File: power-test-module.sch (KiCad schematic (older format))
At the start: 2 parts, among them J3 Conn_01x06, J4 Conn_01x06

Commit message: fixed design-rule issues
 - removed stray via
 - replaced 2 single-row headers by a 2x6 (vertical) header to
   avoid court-yard overlaps.
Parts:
- removed J3, J4: Conn_01x06, Connector_PinHeader_2.54mm:PinHeader_1x06_P2.54mm_Horizontal, symbol Connector_Generic:Conn_01x06
- added J3: Conn_02x06_Odd_Even, Connector_PinHeader_2.54mm:PinHeader_2x06_P2.54mm_Vertical, symbol Connector_Generic:Conn_02x06_Odd_Even
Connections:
- wire segments 17 -> 24
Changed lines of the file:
@@
 $EndSheet
 Wire Wire Line
-	3750 4600 3400 4600
-Wire Wire Line
-	3400 4700 3750 4700
-$Comp
-L power:+3V3 #PWR?
-U 1 1 5C4DEBEA
-P 3750 4300
-AR Path="/5BE73D36/5C4DEBEA" Ref="#PWR?"  Part="1"
-AR Path="/5C1147CA/5C4DEBEA" Ref="#PWR?"  Part="1"
-AR Path="/5C4DEBEA" Ref="#PWR?"  Part="1"
-AR Path="/5C4CE703/5C4DEBEA" Ref="#PWR?"  Part="1"
-F 0 "#PWR?" H 3750 4150 50  0001 C CNN
-F 1 "+3V3" H 3765 4473 50  0000 C CNN
-F 2 "" H 3750 4300 50  0001 C CNN
-F 3 "" H 3750 4300 50  0001 C CNN
-	1    3750 4300
-	1    0    0    -1
-$EndComp
+	2150 3600 1800 3600
+Wire Wire Line
+	1800 3700 2150 3700
 $Comp
 L power:+5V #PWR?
@@
 $EndComp
 $Comp
-L power:+5V #PWR?
-U 1 1 5C4DEC0E
-P 4300 5050
-AR Path="/5C1147CA/5C4DEC0E" Ref="#PWR?"  Part="1"
-AR Path="/5CEAC2F1/5C4DEC0E" Ref="#PWR?"  Part="1"
-AR Path="/5C3C60AE/5C4DEC0E" Ref="#PWR?"  Part="1"
-AR Path="/5C4DEC0E" Ref="#PWR?"  Part="1"
-AR Path="/5C4CE703/5C4DEC0E" Ref="#PWR?"  Part="1"
-F 0 "#PWR?" H 4300 4900 50  0001 C CNN
-F 1 "+5V" H 4315 5223 50  0000 C CNN
-F 2 "" H 4300 5050 50  0001 C CNN
-F 3 "" H 4300 5050 50  0001 C CNN
-	1    4300 5050
-	1    0    0    -1
-$EndComp
-$Comp
 L power:+3V3 #PWR?
 U 1 1 5C4DEC14
@@
 Wire Wire Line
 	5350 4750 4950 4750
-Text Notes 3400 4600 0    25   ~ 0
+Text Notes 1800 3600 0    25   ~ 0
 TXD -> Output
-Text Notes 3400 4700 0    25   ~ 0
+Text Notes 1800 3700 0    25   ~ 0
 RXD <- Input
-Wire Wire Line
-	3750 4400 3750 4300
-Wire Wire Line
-	3750 4500 3750 4400
-Connection ~ 3750 4400
-$Comp
-L Connector_Generic:Conn_01x06 J?
-U 1 1 5C4DEC22
-P 3950 4600
-AR Path="/5C4CE703/5C4DEC22" Ref="J?"  Part="1"
-AR Path="/5C4DEC22" Ref="J3"  Part="1"
-F 0 "J3" H 4030 4592 50  0000 L CNN
-F 1 "Conn_01x06" H 4030 4501 50  0000 L CNN
-F 2 "Connector_PinHeader_2.54mm:PinHeader_1x06_P2.54mm_Horizontal" H 3950 4600 50  0001 C CNN
-F 3 "~" H 3950 4600 50  0001 C CNN
-F 4 "Sullins" H 3950 4600 50  0001 C CNN "Manufacturer"
-F 5 "S5481-ND" H 3950 4600 50  0001 C CNN "Part"
-	1    3950 4600
-	1    0    0    -1
-$EndComp
-Wire Wire Line
-	3750 4800 3650 4800
-Wire Wire Line
-	3650 4800 3650 5000
-Wire Wire Line
-	3750 4900 3750 5000
-Wire Wire Line
-	3750 5050 4300 5050
-$Comp
-L Connector_Generic:Conn_01x06 J?
-U 1 1 5C4DEC2F
-P 4800 3650
-AR Path="/5C4CE703/5C4DEC2F" Ref="J?"  Part="1"
-AR Path="/5C4DEC2F" Ref="J4"  Part="1"
-F 0 "J4" H 4880 3642 50  0000 L CNN
-F 1 "Conn_01x06" H 4880 3551 50  0000 L CNN
-F 2 "Connector_PinHeader_2.54mm:PinHeader_1x06_P2.54mm_Horizontal" H 4800 3650 50  0001 C CNN
-F 3 "~" H 4800 3650 50  0001 C CNN
-F 4 "Sullins" H 4800 3650 50  0001 C CNN "Manufacturer"
-F 5 "S5481-ND" H 4800 3650 50  0001 C CNN "Part"
-	1    4800 3650
-	1    0    0    -1
-$EndComp
-Wire Wire Line
-	3650 5000 3750 5000
-Connection ~ 3750 5000
-Wire Wire Line
-	3750 5000 3750 5050
-$Comp
-L power:GND #PWR?
-U 1 1 5C4DEC39
-P 4600 4100
-AR Path="/5C3C60AE/5C4DEC39" Ref="#PWR?"  Part="1"
-AR Path="/5C4DEC39" Ref="#PWR?"  Part="1"
-AR Path="/5C4CE703/5C4DEC39" Ref="#PWR?"  Part="1"
-F 0 "#PWR?" H 4600 3850 50  0001 C CNN
-F 1 "GND" H 4605 3927 50  0000 C CNN
-F 2 "" H 4600 4100 50  0001 C CNN
-F 3 "" H 4600 4100 50  0001 C CNN
-	1    4600 4100
-	1    0    0    -1
-$EndComp
-Wire Wire Line
-	4600 3450 4600 3550
-Connection ~ 4600 3550
-Wire Wire Line
-	4600 3550 4600 3650
-Connection ~ 4600 3650
-Wire Wire Line
-	4600 3650 4600 3750
-Connection ~ 4600 3750
-Wire Wire Line
-	4600 3750 4600 3850
-Connection ~ 4600 3850
-Wire Wire Line
-	4600 3850 4600 3950
-Connection ~ 4600 3950
-Wire Wire Line
-	4600 3950 4600 4100
-Text GLabel 3400 4600 0    50   Input ~ 0
+Text GLabel 1800 3600 0    50   Input ~ 0
 UART_RX_MIO14
-Text GLabel 3400 4700 0    50   Output ~ 0
+Text GLabel 1800 3700 0    50   Output ~ 0
 UART_TX_MIO15
 $Comp
@@
 	1    0    0    -1
 $EndComp
+$Comp
+L Connector_Generic:Conn_02x06_Odd_Even J3
+U 1 1 60D32371
+P 2350 3600
+F 0 "J3" H 2400 4017 50  0000 C CNN
+F 1 "Conn_02x06_Odd_Even" H 3150 3600 50  0000 C CNN
+F 2 "Connector_PinHeader_2.54mm:PinHeader_2x06_P2.54mm_Vertical" H 2350 3600 50  0001 C CNN
+F 3 "~" H 2350 3600 50  0001 C CNN
+	1    2350 3600
+	1    0    0    -1
+$EndComp
+$Comp
+L power:+3V3 #PWR?
+U 1 1 60D34AD1
+P 2100 3250
+AR Path="/5BE73D36/60D34AD1" Ref="#PWR?"  Part="1"
+AR Path="/5C1147CA/60D34AD1" Ref="#PWR?"  Part="1"
+AR Path="/60D34AD1" Ref="#PWR?"  Part="1"
+AR Path="/5C4CE703/60D34AD1" Ref="#PWR?"  Part="1"
+F 0 "#PWR?" H 2100 3100 50  0001 C CNN
+F 1 "+3V3" H 2115 3423 50  0000 C CNN
+F 2 "" H 2100 3250 50  0001 C CNN
+F 3 "" H 2100 3250 50  0001 C CNN
+	1    2100 3250
+	1    0    0    -1
+$EndComp
+Wire Wire Line
+	2100 3250 2100 3400
+Wire Wire Line
+	2100 3500 2150 3500
+Wire Wire Line
+	2150 3400 2100 3400
+Connection ~ 2100 3400
+Wire Wire Line
+	2100 3400 2100 3500
+$Comp
+L power:GND #PWR?
+U 1 1 60D37922
+P 2700 4000
+AR Path="/5C3C60AE/60D37922" Ref="#PWR?"  Part="1"
+AR Path="/60D37922" Ref="#PWR?"  Part="1"
+AR Path="/5C4CE703/60D37922" Ref="#PWR?"  Part="1"
+F 0 "#PWR?" H 2700 3750 50  0001 C CNN
+F 1 "GND" H 2705 3827 50  0000 C CNN
+F 2 "" H 2700 4000 50  0001 C CNN
+F 3 "" H 2700 4000 50  0001 C CNN
+	1    2700 4000
+	1    0    0    -1
+$EndComp
+Wire Wire Line
+	2650 3400 2700 3400
+Wire Wire Line
+	2700 3400 2700 3500
+Wire Wire Line
+	2650 3900 2700 3900
+Connection ~ 2700 3900
+Wire Wire Line
+	2700 3900 2700 4000
+Wire Wire Line
+	2650 3800 2700 3800
+Connection ~ 2700 3800
+Wire Wire Line
+	2700 3800 2700 3900
+Wire Wire Line
+	2650 3700 2700 3700
+Connection ~ 2700 3700
+Wire Wire Line
+	2700 3700 2700 3800
+Wire Wire Line
+	2650 3600 2700 3600
+Connection ~ 2700 3600
+Wire Wire Line
+	2700 3600 2700 3700
+Wire Wire Line
+	2650 3500 2700 3500
+Connection ~ 2700 3500
+Wire Wire Line
+	2700 3500 2700 3600
+$Comp
+L power:+5V #PWR?
+U 1 1 60D397E5
+P 1650 4150
+AR Path="/5C1147CA/60D397E5" Ref="#PWR?"  Part="1"
+AR Path="/5CEAC2F1/60D397E5" Ref="#PWR?"  Part="1"
+AR Path="/5C3C60AE/60D397E5" Ref="#PWR?"  Part="1"
+AR Path="/60D397E5" Ref="#PWR?"  Part="1"
+AR Path="/5C4CE703/60D397E5" Ref="#PWR?"  Part="1"
+F 0 "#PWR?" H 1650 4000 50  0001 C CNN
+F 1 "+5V" H 1665 4323 50  0000 C CNN
+F 2 "" H 1650 4150 50  0001 C CNN
+F 3 "" H 1650 4150 50  0001 C CNN
+	1    1650 4150
+	1    0    0    -1
+$EndComp
+Wire Wire Line
+	2150 3800 2100 3800
+Wire Wire Line
+	2100 3800 2100 3900
+Wire Wire Line
+	2100 4150 1650 4150
+Wire Wire Line
+	2100 3900 2150 3900
+Connection ~ 2100 3900
+Wire Wire Line
+	2100 3900 2100 4150
 $EndSCHEMATC

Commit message: re-annotated with base number 1000
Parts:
- renumbered J3 to J1001
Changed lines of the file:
@@
 $EndComp
 $Comp
-L Connector_Generic:Conn_02x06_Odd_Even J3
+L Connector_Generic:Conn_02x06_Odd_Even J1001
 U 1 1 60D32371
 P 2350 3600
-F 0 "J3" H 2400 4017 50  0000 C CNN
+F 0 "J1001" H 2400 4017 50  0000 C CNN
 F 1 "Conn_02x06_Odd_Even" H 3150 3600 50  0000 C CNN
 F 2 "Connector_PinHeader_2.54mm:PinHeader_2x06_P2.54mm_Vertical" H 2350 3600 50  0001 C CNN

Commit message: use hierarchical labels from power-and-uart sheet
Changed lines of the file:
@@
 F0 "Sheet5C4CE702" 50
 F1 "power-and-uart.sch" 50
+F2 "UART_TX_OUT" O R 5450 1900 50
+F3 "UART_RX_IN" I L 4100 1900 50
 $EndSheet
 Wire Wire Line
@@
 Wire Wire Line
 	2100 3900 2100 4150
+Text GLabel 5750 1900 2    50   Output ~ 0
+UART_RX_MIO14
+Text GLabel 3700 1900 0    50   Input ~ 0
+UART_TX_MIO15
+Wire Wire Line
+	3700 1900 4100 1900
+Wire Wire Line
+	5450 1900 5750 1900
 $EndSCHEMATC

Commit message: use special +5/+3V3 labels with more specific net names
This allows easier integration since these are global labels
and using more specific names helps avoiding clashes.

The labels are stored in the 'rescue' library.

Strangely: the same trick did not work for GND. Kicad always
insists the net name remains 'GND' (it does work, however if
a new schematic is created - then the different net name for
GND 'sticks').
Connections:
- net +3V3 renamed +3V3_PWR_OUT
- net +5V renamed +5V_PWR_OUT
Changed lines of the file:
@@
 	1800 3700 2150 3700
 $Comp
-L power:+5V #PWR?
+L power-test-module-rescue:+5V #PWR?
 U 1 1 5C4DEBF0
 P 7050 4350
@@
 	1    0    0    -1
 $EndComp
-$Comp
-L power:+3V3 #PWR?
-U 1 1 5C4DEC14
-P 5350 4750
-AR Path="/5BE73D36/5C4DEC14" Ref="#PWR?"  Part="1"
-AR Path="/5C1147CA/5C4DEC14" Ref="#PWR?"  Part="1"
-AR Path="/5C4DEC14" Ref="#PWR?"  Part="1"
-AR Path="/5C4CE703/5C4DEC14" Ref="#PWR?"  Part="1"
-F 0 "#PWR?" H 5350 4600 50  0001 C CNN
-F 1 "+3V3" H 5365 4923 50  0000 C CNN
-F 2 "" H 5350 4750 50  0001 C CNN
-F 3 "" H 5350 4750 50  0001 C CNN
-	1    5350 4750
-	1    0    0    -1
-$EndComp
-Wire Wire Line
-	5350 4750 4950 4750
 Text Notes 1800 3600 0    25   ~ 0
 TXD -> Output
@@
 UART_TX_MIO15
 $Comp
-L trigbox:VIN_3V3 #PWR?
-U 1 1 60D303FF
-P 4950 4750
-F 0 "#PWR?" H 4950 4600 50  0001 C CNN
-F 1 "VIN_3V3" H 4965 4923 50  0000 C CNN
-F 2 "" H 4950 4750 50  0001 C CNN
-F 3 "" H 4950 4750 50  0001 C CNN
-	1    4950 4750
-	1    0    0    -1
-$EndComp
-$Comp
 L Connector_Generic:Conn_02x06_Odd_Even J1001
 U 1 1 60D32371
@@
 $EndComp
 $Comp
-L power:+3V3 #PWR?
+L power-test-module-rescue:+3V3 #PWR?
 U 1 1 60D34AD1
 P 2100 3250
@@
 	2700 3500 2700 3600
 $Comp
-L power:+5V #PWR?
+L power-test-module-rescue:+5V #PWR?
 U 1 1 60D397E5
 P 1650 4150
@@
 Wire Wire Line
 	5450 1900 5750 1900
+$Comp
+L power-test-module-rescue:+3V3 #PWR?
+U 1 1 60DA6E5B
+P 6400 4350
+AR Path="/5BE73D36/60DA6E5B" Ref="#PWR?"  Part="1"
+AR Path="/5C1147CA/60DA6E5B" Ref="#PWR?"  Part="1"
+AR Path="/60DA6E5B" Ref="#PWR?"  Part="1"
+AR Path="/5C4CE703/60DA6E5B" Ref="#PWR?"  Part="1"
+F 0 "#PWR?" H 6400 4200 50  0001 C CNN
+F 1 "+3V3" H 6415 4523 50  0000 C CNN
+F 2 "" H 6400 4350 50  0001 C CNN
+F 3 "" H 6400 4350 50  0001 C CNN
+	1    6400 4350
+	1    0    0    -1
+$EndComp
+$Comp
+L power:PWR_FLAG #FLG?
+U 1 1 60DA70DA
+P 6400 4350
+AR Path="/5C3C60AE/60DA70DA" Ref="#FLG?"  Part="1"
+AR Path="/60DA70DA" Ref="#FLG?"  Part="1"
+AR Path="/5C4CE703/60DA70DA" Ref="#FLG?"  Part="1"
+F 0 "#FLG?" H 6400 4425 50  0001 C CNN
+F 1 "PWR_FLAG" H 6400 4524 50  0000 C CNN
+F 2 "" H 6400 4350 50  0001 C CNN
+F 3 "~" H 6400 4350 50  0001 C CNN
+	1    6400 4350
+	1    0    0    1
+$EndComp
 $EndSCHEMATC

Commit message: removed global labels for UART-TX/RX
There referred to MIO pins on the CPU board which don't really
belong here; also: avoid global labels for a module.
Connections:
- net UART_RX_MIO14 renamed UART_TX_OUT
- net UART_TX_MIO15 renamed UART_RX_IN
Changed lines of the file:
@@
 Text Notes 1800 3700 0    25   ~ 0
 RXD <- Input
-Text GLabel 1800 3600 0    50   Input ~ 0
-UART_RX_MIO14
-Text GLabel 1800 3700 0    50   Output ~ 0
-UART_TX_MIO15
 $Comp
 L Connector_Generic:Conn_02x06_Odd_Even J1001
@@
 Wire Wire Line
 	2100 3900 2100 4150
-Text GLabel 5750 1900 2    50   Output ~ 0
-UART_RX_MIO14
-Text GLabel 3700 1900 0    50   Input ~ 0
-UART_TX_MIO15
 Wire Wire Line
 	3700 1900 4100 1900
@@
 	1    0    0    1
 $EndComp
+Text Label 5750 1900 0    50   ~ 0
+UART_TX_OUT
+Text Label 1800 3600 2    50   ~ 0
+UART_TX_OUT
+Text Label 3700 1900 2    50   ~ 0
+UART_RX_IN
+Text Label 1800 3700 2    50   ~ 0
+UART_RX_IN
 $EndSCHEMATC

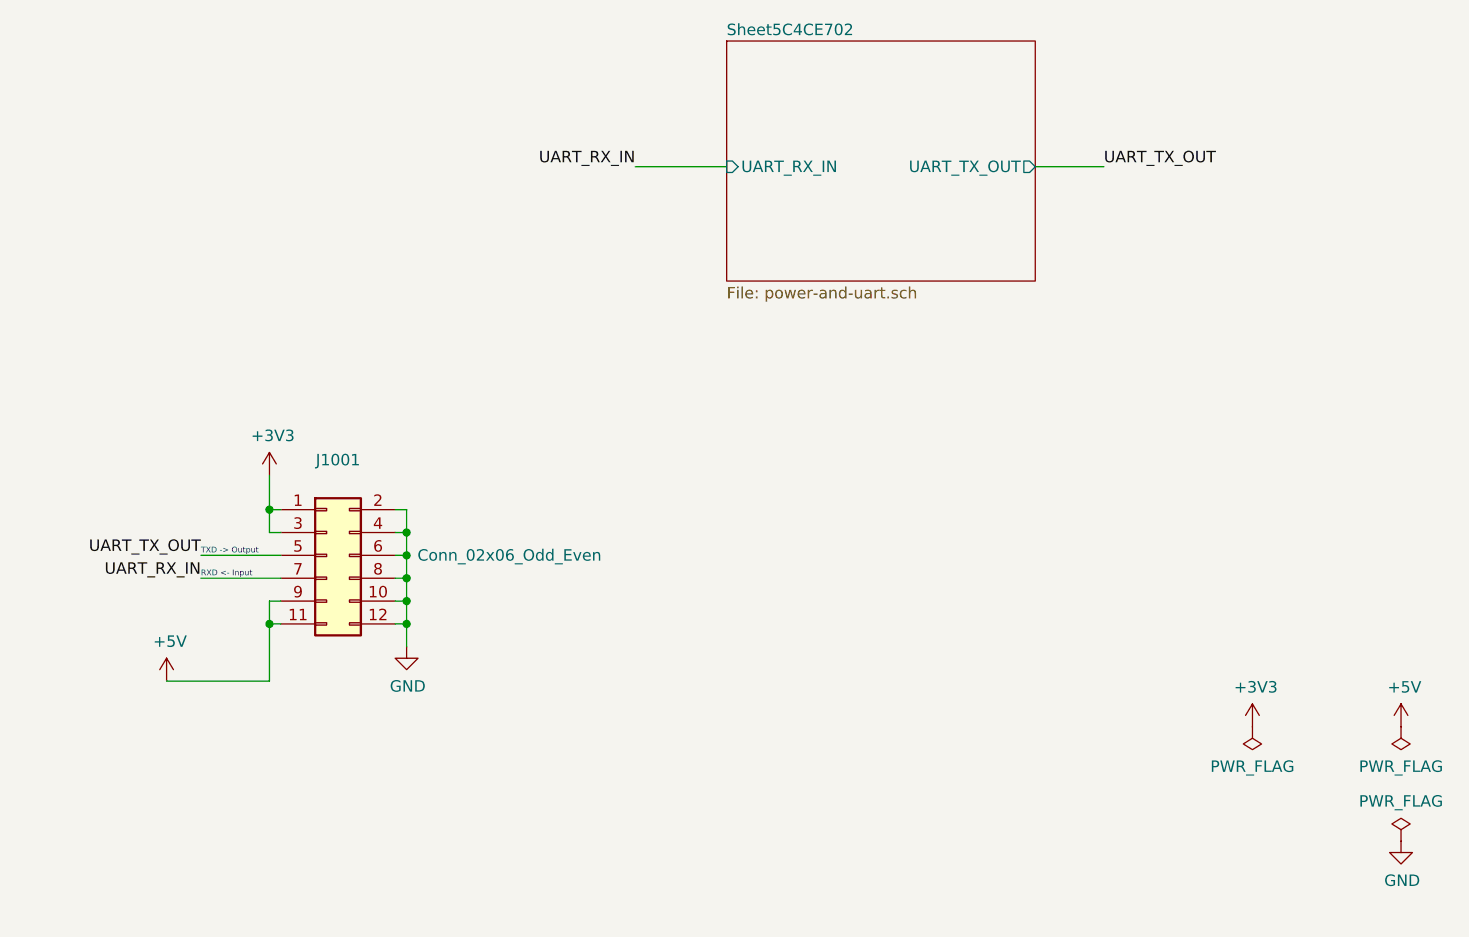
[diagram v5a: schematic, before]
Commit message: replaced PMOD connector by hierarchical sheet labels; removed power flags
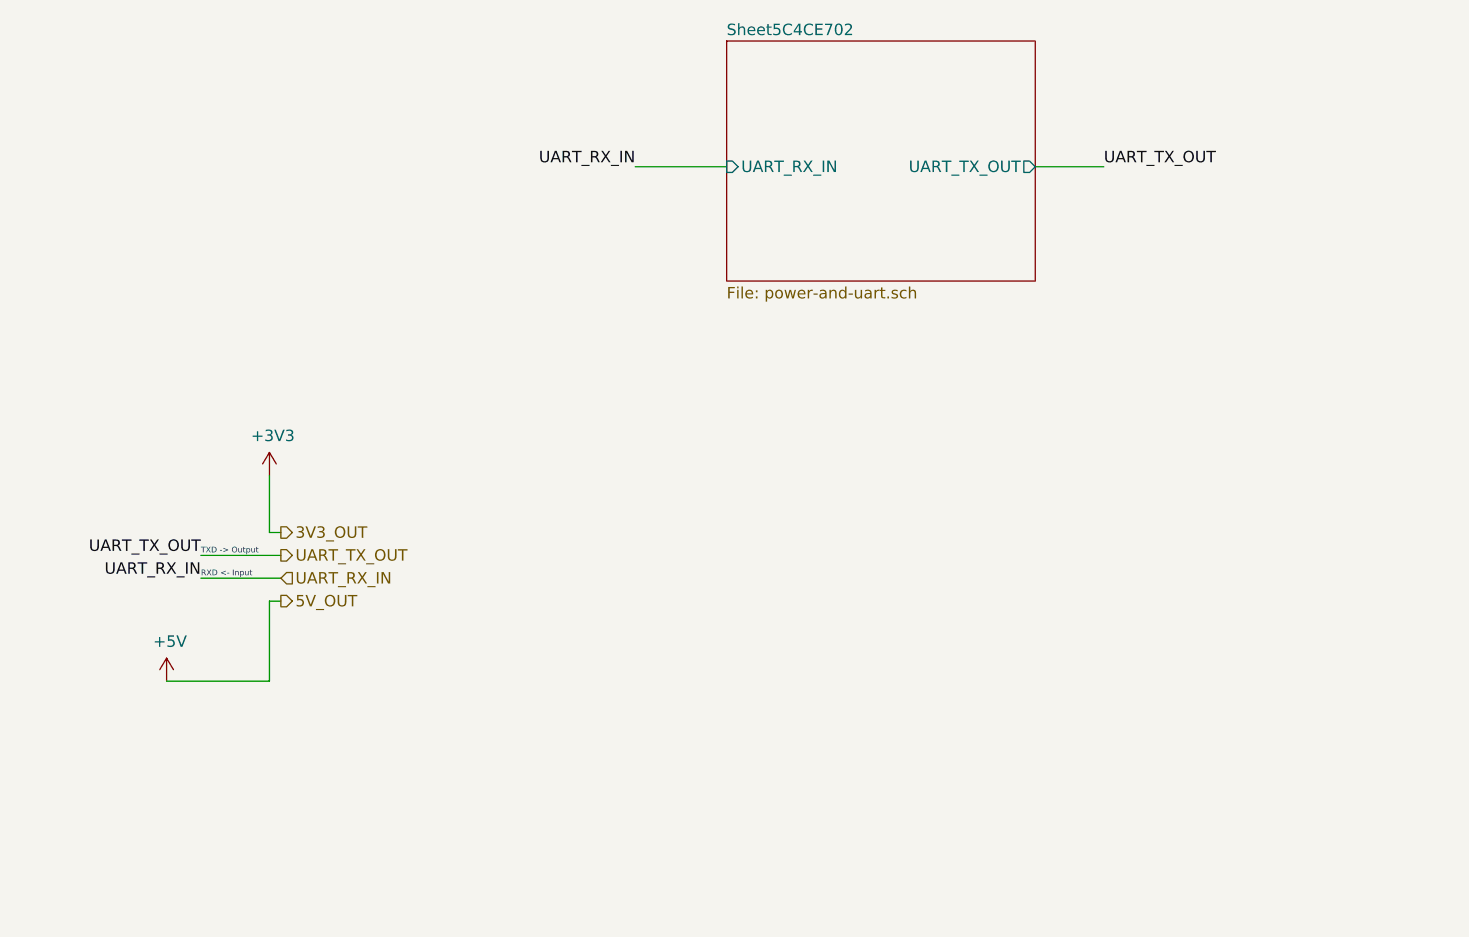
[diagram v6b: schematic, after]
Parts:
- removed J1001: Conn_02x06_Odd_Even, Connector_PinHeader_2.54mm:PinHeader_2x06_P2.54mm_Vertical, symbol Connector_Generic:Conn_02x06_Odd_Even
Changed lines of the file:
@@
 Wire Wire Line
 	1800 3700 2150 3700
-$Comp
-L power-test-module-rescue:+5V #PWR?
-U 1 1 5C4DEBF0
-P 7050 4350
-AR Path="/5C1147CA/5C4DEBF0" Ref="#PWR?"  Part="1"
-AR Path="/5CEAC2F1/5C4DEBF0" Ref="#PWR?"  Part="1"
-AR Path="/5C3C60AE/5C4DEBF0" Ref="#PWR?"  Part="1"
-AR Path="/5C4DEBF0" Ref="#PWR?"  Part="1"
-AR Path="/5C4CE703/5C4DEBF0" Ref="#PWR?"  Part="1"
-F 0 "#PWR?" H 7050 4200 50  0001 C CNN
-F 1 "+5V" H 7065 4523 50  0000 C CNN
-F 2 "" H 7050 4350 50  0001 C CNN
-F 3 "" H 7050 4350 50  0001 C CNN
-	1    7050 4350
-	1    0    0    -1
-$EndComp
-$Comp
-L power:PWR_FLAG #FLG?
-U 1 1 5C4DEBF6
-P 7050 4350
-AR Path="/5C3C60AE/5C4DEBF6" Ref="#FLG?"  Part="1"
-AR Path="/5C4DEBF6" Ref="#FLG?"  Part="1"
-AR Path="/5C4CE703/5C4DEBF6" Ref="#FLG?"  Part="1"
-F 0 "#FLG?" H 7050 4425 50  0001 C CNN
-F 1 "PWR_FLAG" H 7050 4524 50  0000 C CNN
-F 2 "" H 7050 4350 50  0001 C CNN
-F 3 "~" H 7050 4350 50  0001 C CNN
-	1    7050 4350
-	1    0    0    1
-$EndComp
-$Comp
-L power:GND #PWR?
-U 1 1 5C4DEBFC
-P 7050 4850
-AR Path="/5C3C60AE/5C4DEBFC" Ref="#PWR?"  Part="1"
-AR Path="/5C4DEBFC" Ref="#PWR?"  Part="1"
-AR Path="/5C4CE703/5C4DEBFC" Ref="#PWR?"  Part="1"
-F 0 "#PWR?" H 7050 4600 50  0001 C CNN
-F 1 "GND" H 7055 4677 50  0000 C CNN
-F 2 "" H 7050 4850 50  0001 C CNN
-F 3 "" H 7050 4850 50  0001 C CNN
-	1    7050 4850
-	1    0    0    -1
-$EndComp
-$Comp
-L power:PWR_FLAG #FLG?
-U 1 1 5C4DEC02
-P 7050 4850
-AR Path="/5C3C60AE/5C4DEC02" Ref="#FLG?"  Part="1"
-AR Path="/5C4DEC02" Ref="#FLG?"  Part="1"
-AR Path="/5C4CE703/5C4DEC02" Ref="#FLG?"  Part="1"
-F 0 "#FLG?" H 7050 4925 50  0001 C CNN
-F 1 "PWR_FLAG" H 7050 5024 50  0000 C CNN
-F 2 "" H 7050 4850 50  0001 C CNN
-F 3 "~" H 7050 4850 50  0001 C CNN
-	1    7050 4850
-	1    0    0    -1
-$EndComp
 Text Notes 1800 3600 0    25   ~ 0
 TXD -> Output
 Text Notes 1800 3700 0    25   ~ 0
 RXD <- Input
-$Comp
-L Connector_Generic:Conn_02x06_Odd_Even J1001
-U 1 1 60D32371
-P 2350 3600
-F 0 "J1001" H 2400 4017 50  0000 C CNN
-F 1 "Conn_02x06_Odd_Even" H 3150 3600 50  0000 C CNN
-F 2 "Connector_PinHeader_2.54mm:PinHeader_2x06_P2.54mm_Vertical" H 2350 3600 50  0001 C CNN
-F 3 "~" H 2350 3600 50  0001 C CNN
-	1    2350 3600
-	1    0    0    -1
-$EndComp
 $Comp
 L power-test-module-rescue:+3V3 #PWR?
@@
 $EndComp
 Wire Wire Line
-	2100 3250 2100 3400
-Wire Wire Line
 	2100 3500 2150 3500
-Wire Wire Line
-	2150 3400 2100 3400
-Connection ~ 2100 3400
-Wire Wire Line
-	2100 3400 2100 3500
-$Comp
-L power:GND #PWR?
-U 1 1 60D37922
-P 2700 4000
-AR Path="/5C3C60AE/60D37922" Ref="#PWR?"  Part="1"
-AR Path="/60D37922" Ref="#PWR?"  Part="1"
-AR Path="/5C4CE703/60D37922" Ref="#PWR?"  Part="1"
-F 0 "#PWR?" H 2700 3750 50  0001 C CNN
-F 1 "GND" H 2705 3827 50  0000 C CNN
-F 2 "" H 2700 4000 50  0001 C CNN
-F 3 "" H 2700 4000 50  0001 C CNN
-	1    2700 4000
-	1    0    0    -1
-$EndComp
-Wire Wire Line
-	2650 3400 2700 3400
-Wire Wire Line
-	2700 3400 2700 3500
-Wire Wire Line
-	2650 3900 2700 3900
-Connection ~ 2700 3900
-Wire Wire Line
-	2700 3900 2700 4000
-Wire Wire Line
-	2650 3800 2700 3800
-Connection ~ 2700 3800
-Wire Wire Line
-	2700 3800 2700 3900
-Wire Wire Line
-	2650 3700 2700 3700
-Connection ~ 2700 3700
-Wire Wire Line
-	2700 3700 2700 3800
-Wire Wire Line
-	2650 3600 2700 3600
-Connection ~ 2700 3600
-Wire Wire Line
-	2700 3600 2700 3700
-Wire Wire Line
-	2650 3500 2700 3500
-Connection ~ 2700 3500
-Wire Wire Line
-	2700 3500 2700 3600
 $Comp
 L power-test-module-rescue:+5V #PWR?
@@
 	2150 3800 2100 3800
 Wire Wire Line
-	2100 3800 2100 3900
-Wire Wire Line
 	2100 4150 1650 4150
-Wire Wire Line
-	2100 3900 2150 3900
-Connection ~ 2100 3900
-Wire Wire Line
-	2100 3900 2100 4150
 Wire Wire Line
 	3700 1900 4100 1900
 Wire Wire Line
 	5450 1900 5750 1900
-$Comp
-L power-test-module-rescue:+3V3 #PWR?
-U 1 1 60DA6E5B
-P 6400 4350
-AR Path="/5BE73D36/60DA6E5B" Ref="#PWR?"  Part="1"
-AR Path="/5C1147CA/60DA6E5B" Ref="#PWR?"  Part="1"
-AR Path="/60DA6E5B" Ref="#PWR?"  Part="1"
-AR Path="/5C4CE703/60DA6E5B" Ref="#PWR?"  Part="1"
-F 0 "#PWR?" H 6400 4200 50  0001 C CNN
-F 1 "+3V3" H 6415 4523 50  0000 C CNN
-F 2 "" H 6400 4350 50  0001 C CNN
-F 3 "" H 6400 4350 50  0001 C CNN
-	1    6400 4350
-	1    0    0    -1
-$EndComp
-$Comp
-L power:PWR_FLAG #FLG?
-U 1 1 60DA70DA
-P 6400 4350
-AR Path="/5C3C60AE/60DA70DA" Ref="#FLG?"  Part="1"
-AR Path="/60DA70DA" Ref="#FLG?"  Part="1"
-AR Path="/5C4CE703/60DA70DA" Ref="#FLG?"  Part="1"
-F 0 "#FLG?" H 6400 4425 50  0001 C CNN
-F 1 "PWR_FLAG" H 6400 4524 50  0000 C CNN
-F 2 "" H 6400 4350 50  0001 C CNN
-F 3 "~" H 6400 4350 50  0001 C CNN
-	1    6400 4350
-	1    0    0    1
-$EndComp
 Text Label 5750 1900 0    50   ~ 0
 UART_TX_OUT
@@
 Text Label 1800 3700 2    50   ~ 0
 UART_RX_IN
+Wire Wire Line
+	2100 3800 2100 4150
+Wire Wire Line
+	2100 3250 2100 3500
+Text HLabel 2150 3500 2    50   Output ~ 0
+3V3_OUT
+Text HLabel 2150 3800 2    50   Output ~ 0
+5V_OUT
+Text HLabel 2150 3600 2    50   Output ~ 0
+UART_TX_OUT
+Text HLabel 2150 3700 2    50   Input ~ 0
+UART_RX_IN
 $EndSCHEMATC
